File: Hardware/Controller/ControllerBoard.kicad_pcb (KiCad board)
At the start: 4 copper layers, 45 x 42.5 mm, 62 parts, among them J1 Conn_01x08_MountingPin, J2 USB_C_Receptacle_USB2.0, J3 Conn_01x02_Male, J4 Interface, J5 I2C, J6 I2C ThroughHole, Q1 BC818, Q2 AO3401A, Q3 BC818, Q4 AO3401A, U1 ESP32-S3-WROOM-1, U2 SN65220, U3 TLV62569DBV, U5 MCP73811T-420I-OT, X1 CON_JST_PH_2PIN_MTPH2

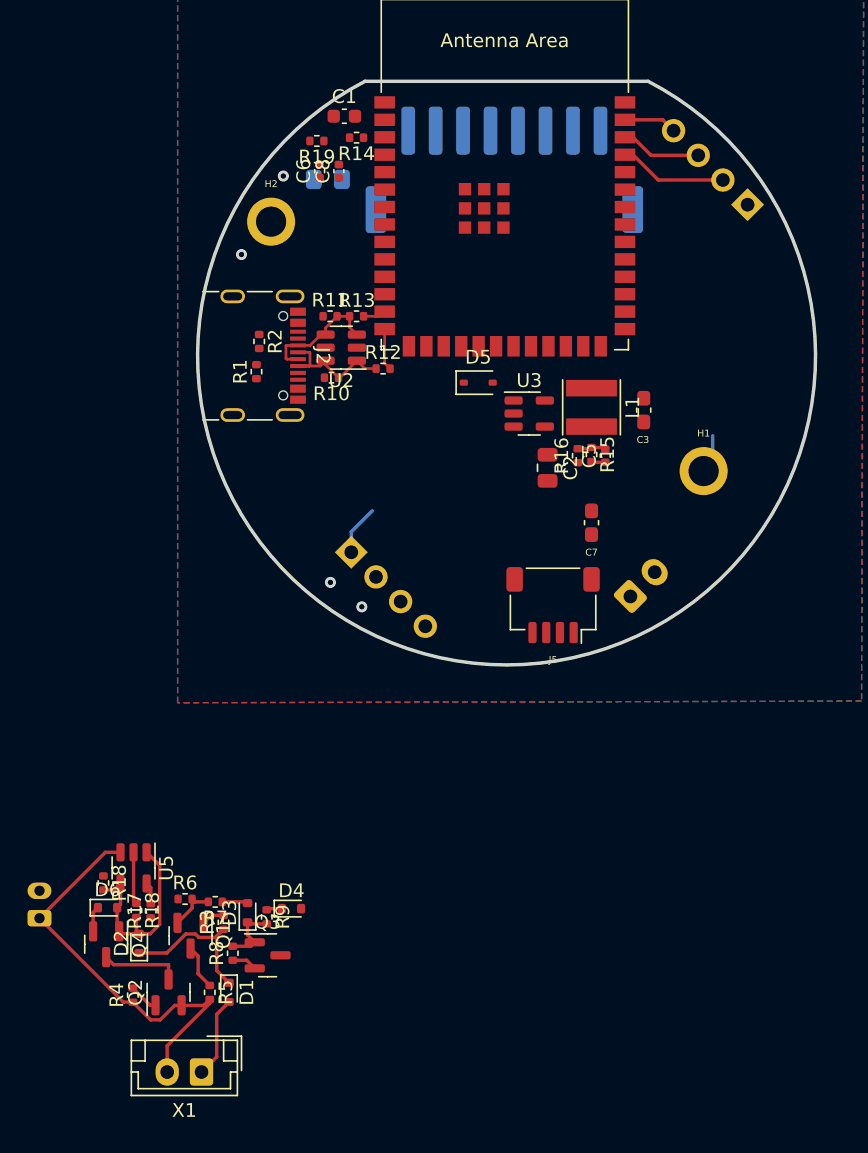
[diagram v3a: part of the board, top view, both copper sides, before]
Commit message: updated routing on control board, added led pcb template
Signed-off-by: lokimetasmith <lokimail@gmail.com>
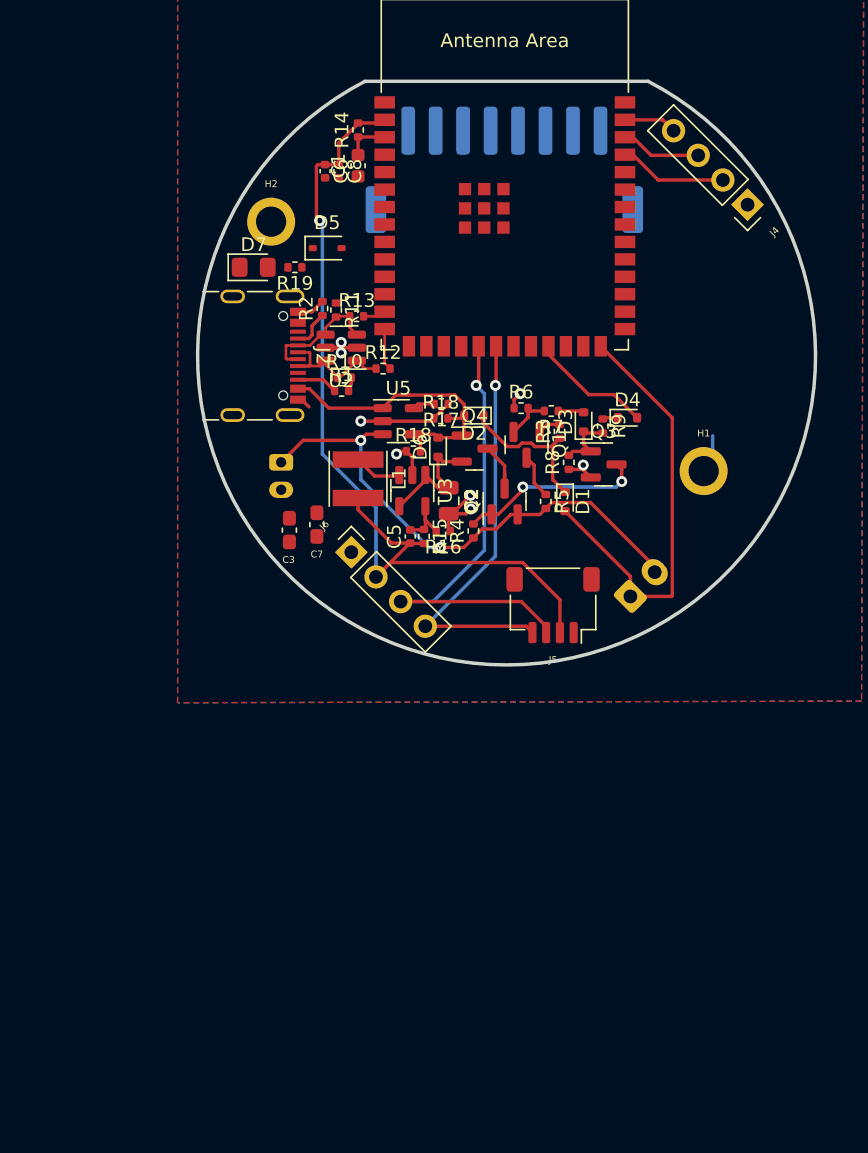
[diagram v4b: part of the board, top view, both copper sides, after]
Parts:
- removed the X1 at (159.6, 113.2)
- D7, J4, J6: moved to F.Cu
- moved D2 45.5 mm to (179.4, 65.4), turned to 180 degrees
- moved Q4 45.0 mm to (179.5, 67.8), turned to 0 degrees
- moved D1 43.3 mm to (186.1, 71.7)
- moved Q2 43.3 mm to (181.7, 71.7)
- moved Q3 43.3 mm to (188.9, 69.0)
- moved R5 43.3 mm to (184.7, 71.7)
- moved R7 43.3 mm to (185.1, 65.1)
- moved R9 43.3 mm to (188.8, 66.2)
- moved D3 43.3 mm to (187.4, 65.9)
- moved D4 43.3 mm to (190.6, 65.6)
- moved Q1 43.3 mm to (183.3, 67.5)
- moved R3 43.3 mm to (185.7, 66.6)
- moved R6 43.3 mm to (182.9, 64.9)
- moved R8 43.3 mm to (186.3, 68.8)
- moved R17 42.5 mm to (177.1, 64.6), turned to 180 degrees
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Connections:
- net USB_pwr renamed /USB_pwr
- J5 pad 2: VCC -> +3V3
- J6 pad 2: VCC -> +3V3
- U1 pad 2: 3.3V -> +3V3
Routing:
- net +3V3: track 7.10 -> 66.5 mm, vias 0 -> 1
- net SDA: track 0.00 -> 34.6 mm, vias 0 -> 1
- net SCL: track 0.00 -> 30.5 mm, vias 0 -> 1
- net /Trigger: track 5.93 -> 31.6 mm
- net GND: track 10.5 -> 27.7 mm, vias 4 -> 8
- net Net-(Q2-G): track 2.17 -> 13.6 mm, vias 0 -> 2
- net /KeepAlive: track 0.00 -> 8.95 mm
- net /Trigger_Wake_Up/VBAT: track 30.5 -> 38.7 mm, vias 0 -> 2
- net /Switched_Power: track 1.87 -> 9.59 mm
- net /USB_pwr: track 15.8 -> 21.7 mm
- net Net-(U3-SW): track 0.00 -> 3.53 mm
- net /EN: track 0.00 -> 3.26 mm
- net Net-(J2-CC2): track 0.00 -> 3.00 mm
- net Net-(J2-CC1): track 0.00 -> 2.87 mm
- net Net-(U3-FB): track 2.09 -> 4.87 mm
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- removed copper zone on In2.Cu, net +3V3
- removed copper zone on In1.Cu, net GND
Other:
- copper layers 4 -> 2

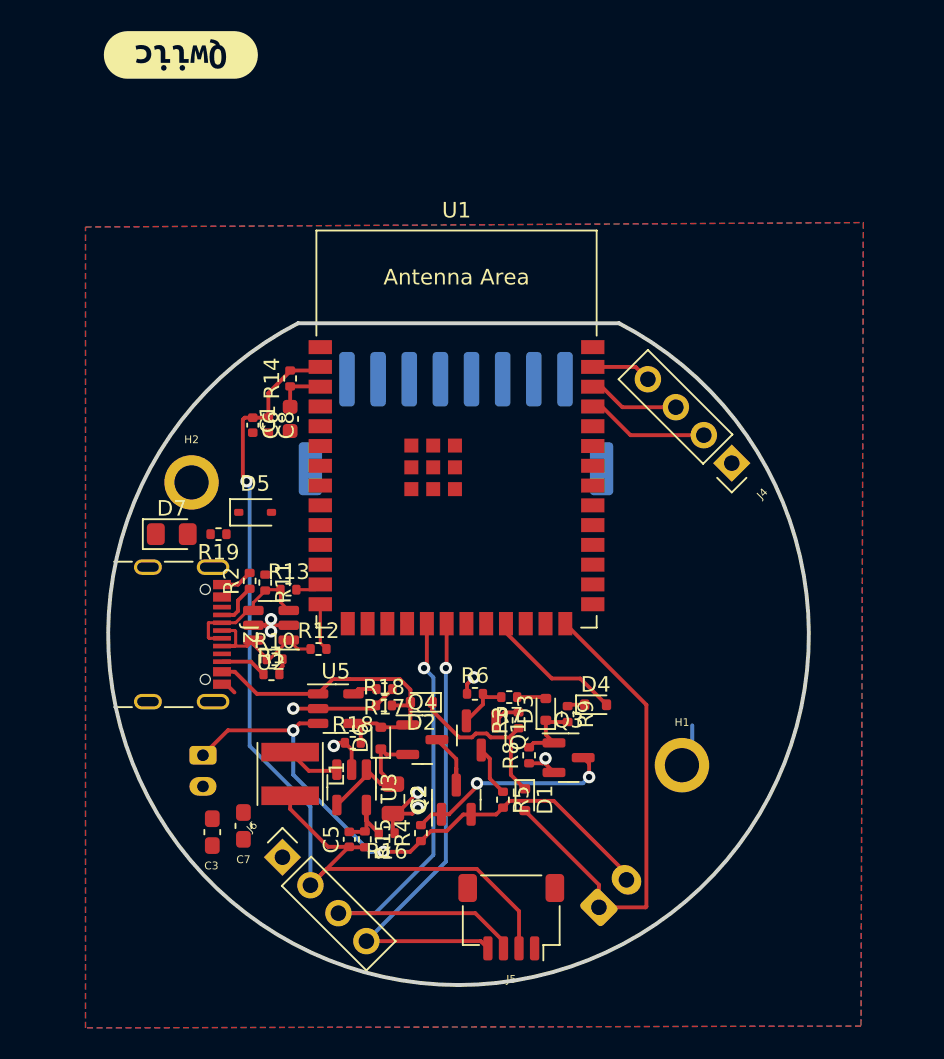
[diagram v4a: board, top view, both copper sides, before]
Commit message: as ordered 11/27/2023 from JLCPCB
Updated silk on RoundScanner, minor changes,

major changes on control board, cleaned up foot prints, nudged parts around
control board not ready for release yet
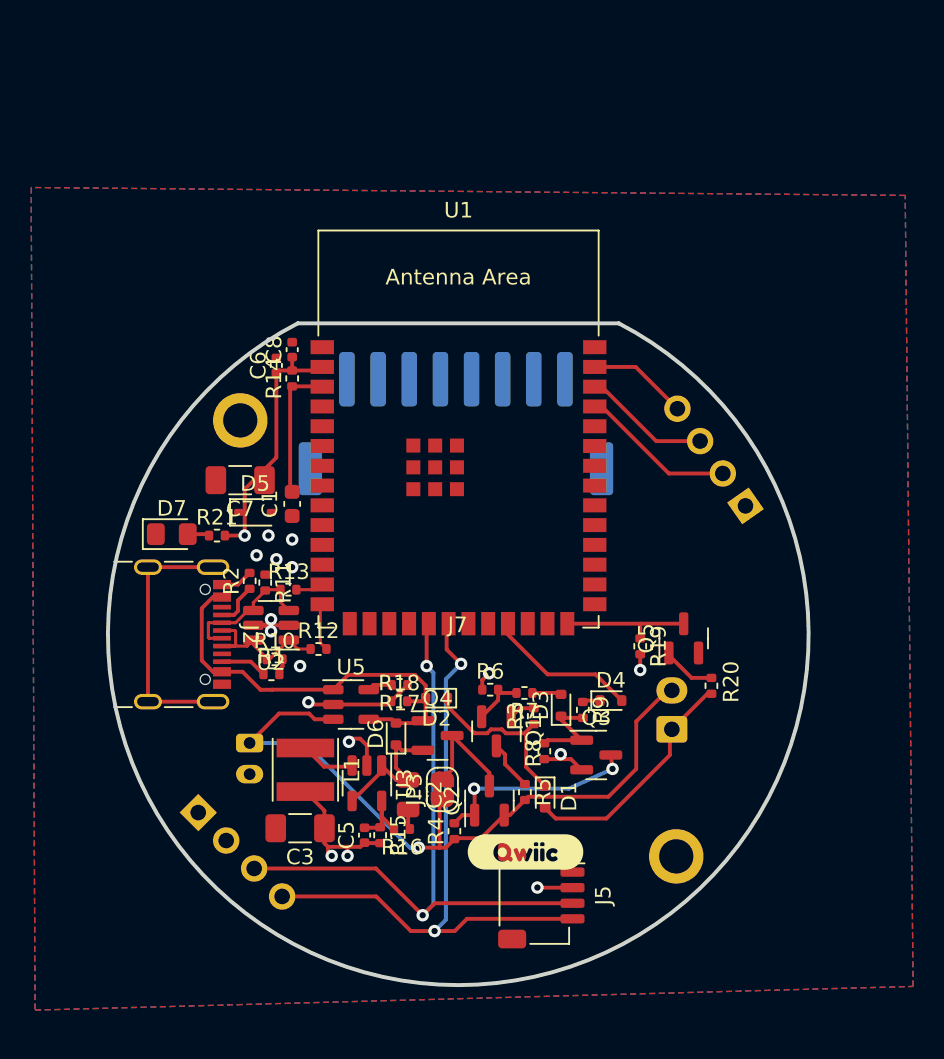
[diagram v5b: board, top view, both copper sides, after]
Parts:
- removed H1, H2: MountingHole, MountingHole:MountingHole_2.2mm_M2_ISO7380_Pad
- removed J4: Interface, Connector_PinSocket_2.54mm:PinSocket_1x04_P2.54mm_Vertical
- removed J6: I2C ThroughHole, Connector_PinSocket_2.54mm:PinSocket_1x04_P2.54mm_Vertical
- removed OSH logo: OSHW-Logo2_9.8x8mm_SilkScreen, Symbol:OSHW-Logo2_9.8x8mm_SilkScreen
- removed PlasticScannerLogo: PlasticScannerLogo, Symbol:PlasticScannerLogo
- removed the R18 at (175.0, 68.0)
- removed kibuzzard-639881D9: G***, kibuzzard-639881D9
- removed kibuzzard-63988507 (x2): G***, kibuzzard-63988507
- added J7: Conn_01x09, round_module:round_notch, F.Cu at (181.8, 61.3)
- added JP3: Jumper_2_Open, Jumper:SolderJumper-2_P1.3mm_Bridged2Bar_RoundedPad1.0x1.5mm, F.Cu at (180.8, 71.0)
- added Q5: BC818, Package_TO_SOT_SMD:SOT-23, F.Cu at (196.3, 61.3)
- added R20: 1k, Resistor_SMD:R_0402_1005Metric, F.Cu at (198.1, 64.3)
- added R21: 1k, Resistor_SMD:R_0402_1005Metric, F.Cu at (166.3, 54.7)
- C3: value 51pF -> 10u; footprint Capacitor_SMD:C_0603_1608Metric_Pad1.08x0.95mm_HandSolder -> Capacitor_SMD:C_1206_3216Metric_Pad1.33x1.80mm_HandSolder
- C7: value 0.1uF -> 10u; footprint Capacitor_SMD:C_0603_1608Metric_Pad1.08x0.95mm_HandSolder -> Capacitor_SMD:C_1206_3216Metric_Pad1.33x1.80mm_HandSolder
- R19: value 150 -> 10K
- kibuzzard-6398DD41: moved to F.Cu
- moved LOGO2 55.8 mm to (188.1, 66.1)
- moved LOGO1 55.2 mm to (172.7, 58.5)
- moved kibuzzard-6398DD41 44.1 mm to (186.1, 75.0), turned to 0 degrees
- moved kibuzzard-6346913B 33.5 mm to (189.9, 57.2)
- moved R19 28.0 mm to (193.5, 61.8), turned to -90 degrees
- moved C7 22.2 mm to (167.8, 51.1), turned to 180 degrees
- moved X1 12.4 mm to (195.5, 67.1), turned to 90 degrees
- moved C3 5.64 mm to (171.6, 73.5), turned to 180 degrees
- moved C1 5.46 mm to (171.1, 52.7)
- moved C8 5.08 mm to (171.1, 42.8), turned to 90 degrees
- moved C6 4.12 mm to (170.1, 43.8), turned to 90 degrees
- moved J3 3.10 mm to (168.4, 68.0)
- moved J5 2.38 mm to (187.1, 77.8), turned to -90 degrees
- moved R4 2.15 mm to (181.5, 73.7)
- moved Q2 2.13 mm to (183.8, 71.7)
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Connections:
- C3 pad 1: (no net) -> +3V3
- C3 pad 2: (no net) -> GND
- C7 pad 1: GND -> +3V3
- C7 pad 2: (no net) -> GND
- D1 pad 2: /Trigger -> Net-(D1-A)
- J5 pad MP: (no net) -> GND
- R19 pad 1: +3V3 -> /Trigger
- R19 pad 2: Net-(D7-A) -> +3V3
- U1 pad 37: LED RESET -> /LED_RESET
- U1 pad 38: AS7341_INT -> /AS7341_INT
- U1 pad 39: DRDY_INT -> /DRDY_INT
- X1 pad 1: /Trigger -> Net-(D1-A)
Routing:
- net +3V3: track 66.5 -> 28.3 mm, vias 1 -> 5
- net /Trigger: track 31.6 -> 8.54 mm
- net /Shield: track 0.00 -> 17.0 mm
- net Net-(D1-A): track 0.00 -> 15.2 mm
- net SCL: track 30.5 -> 40.7 mm, vias 1 -> 2
- net /LED_RESET: track 0.00 -> 9.55 mm
- net /AS7341_INT: track 0.00 -> 7.76 mm
- net LED RESET: track 7.31 -> 0.00 mm
- net SDA: track 34.6 -> 41.2 mm, vias 1 -> 2
- net /DRDY_INT: track 0.00 -> 6.55 mm
- net /Trigger_Wake_Up/VBAT: track 38.7 -> 44.7 mm, vias 2 -> 1
- net GND: track 27.7 -> 22.4 mm, vias 8 -> 12
- net AS7341_INT: track 5.30 -> 0.00 mm
- net /EN: track 3.26 -> 8.56 mm
- net /USB_pwr: track 21.7 -> 27.0 mm
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- added copper zone on In1.Cu, net +3V3
- added copper zone on In2.Cu, net GND
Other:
- copper layers 2 -> 4
- board text removed: "Power"
